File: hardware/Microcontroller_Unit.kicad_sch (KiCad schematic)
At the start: 30 parts

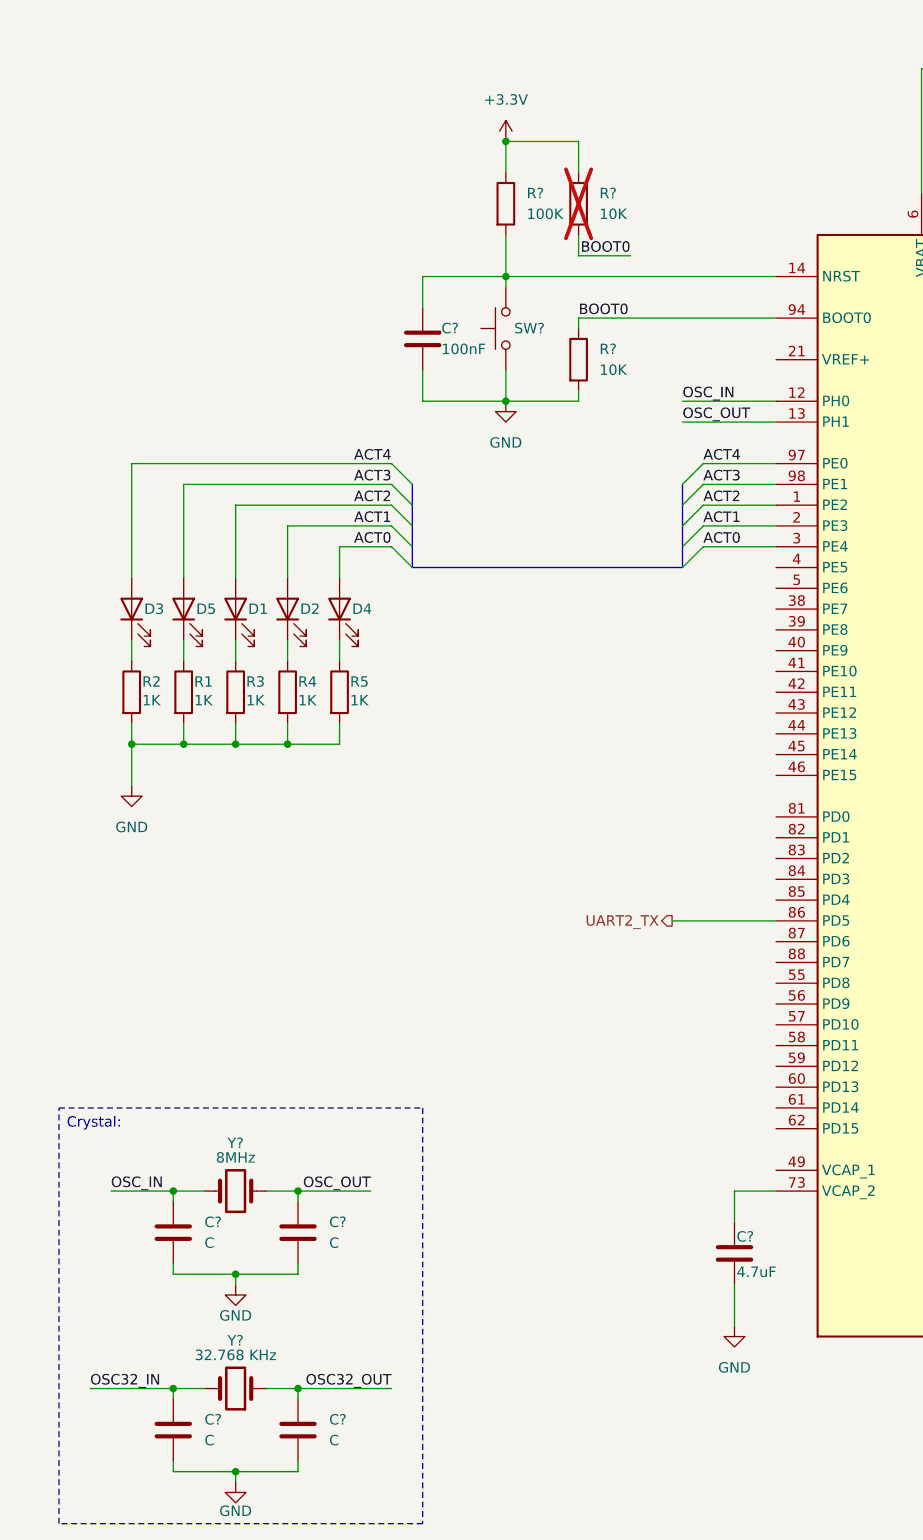
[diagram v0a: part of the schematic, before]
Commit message: Change ESP32 module to stand-alone, change regulator for wide input range, modify location of certain things on MCU_Unit.
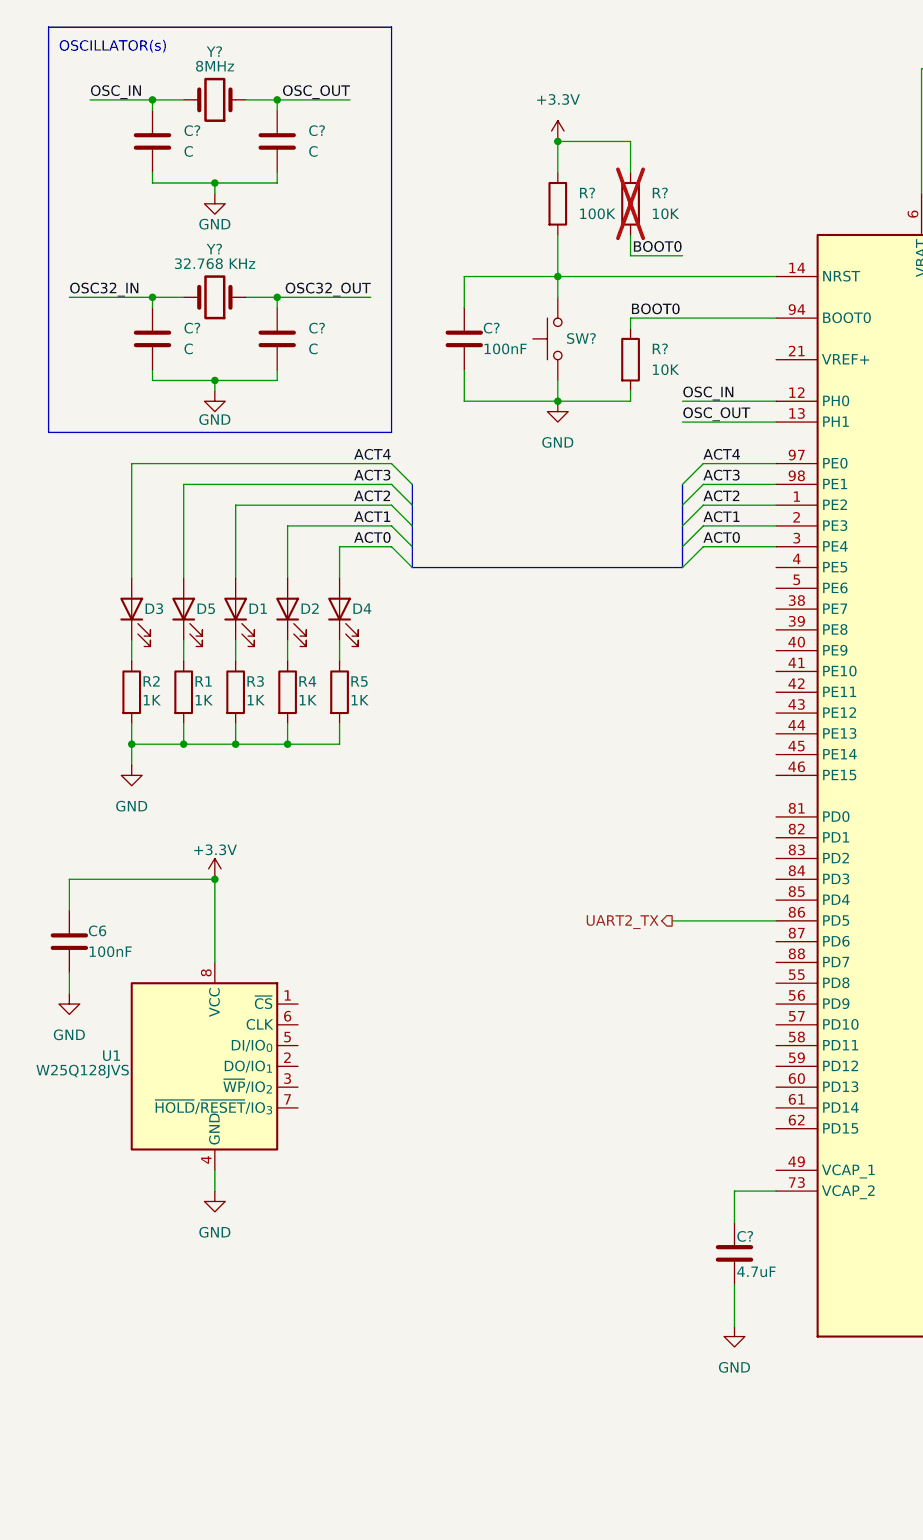
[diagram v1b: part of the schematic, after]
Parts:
- added C6: 100nF, Capacitor_SMD:C_0805_2012Metric_Pad1.18x1.45mm_HandSolder, symbol Device:C
- added R2: 1K, symbol Device:R
- added U1: W25Q128JVS, Package_SO:SOIC-8_5.3x5.3mm_P1.27mm, symbol Memory_Flash:W25Q128JVS
- R?: renamed from R2; value 1K -> 10K
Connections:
- net +3.3V: now also C6.1, U1.8 (VCC)
- net GND: now also C6.2, R2.2, U1.4 (GND)
- net at D3.1 (K): now also R2.1; no longer R?.1
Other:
- note added: "OSCILLATOR(s)"
- moved on the sheet: C?, R?, SW?, Y?

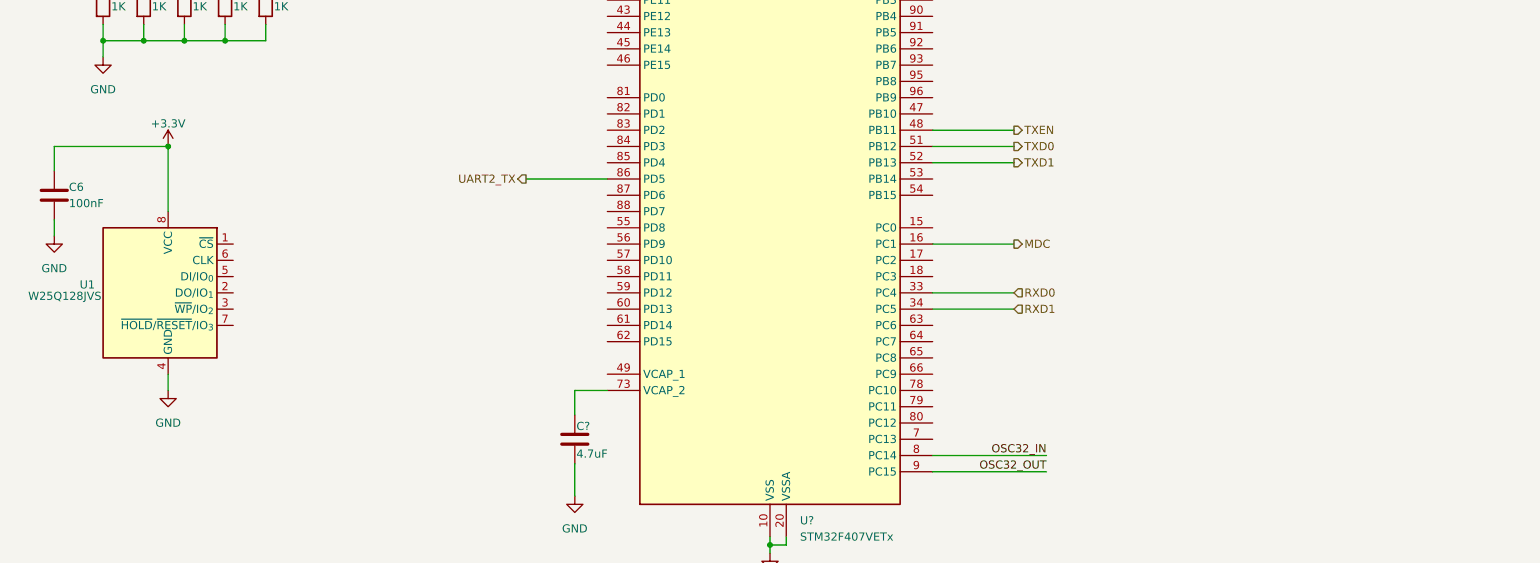
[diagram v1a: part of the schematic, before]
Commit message: Add Flash.
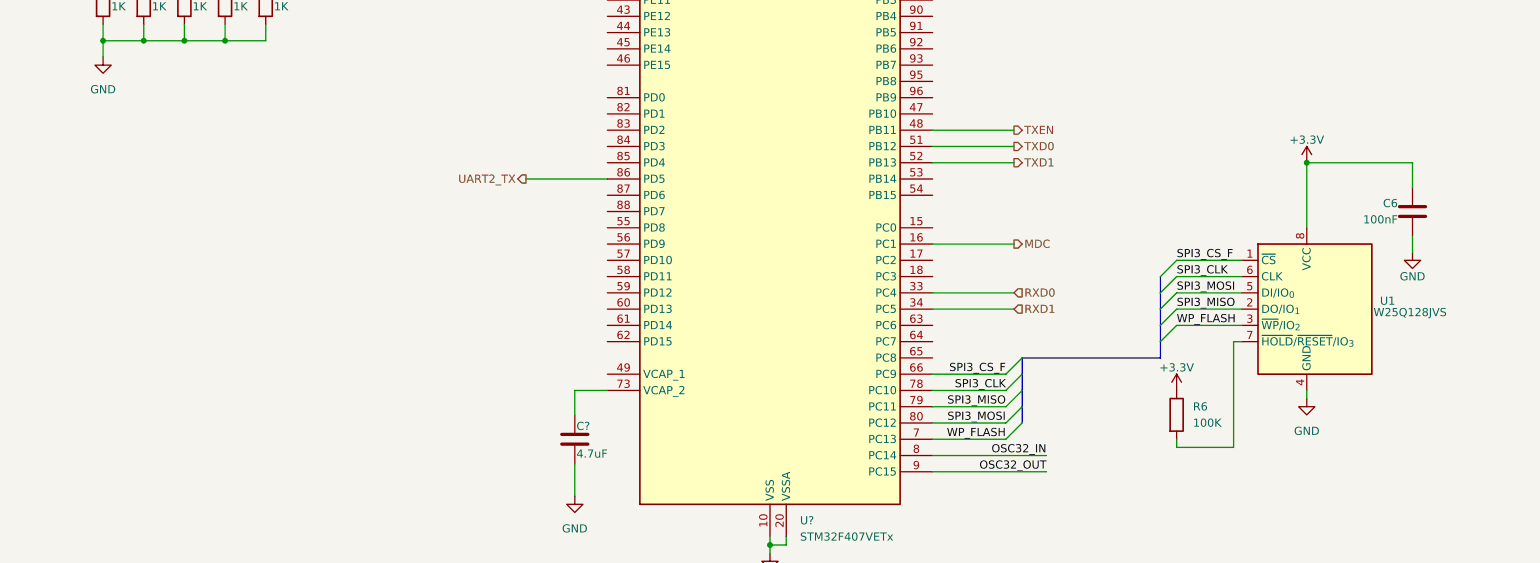
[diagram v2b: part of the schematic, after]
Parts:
- added R6: 100K, symbol Device:R
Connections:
- net +3.3V: now also R6.1
- net SPI3_CS_F: now reaches U?.66 (PC9)
- net SPI3_CS_F: now also U1.1 (~{CS})
- net WP_FLASH: now reaches U?.7 (PC13)
- net WP_FLASH: now also U1.3 (~{WP}/IO_{2})
- net SPI3_CLK: now reaches U?.78 (PC10)
- net SPI3_CLK: now also U1.6 (CLK)
- net SPI3_MISO: now reaches U?.79 (PC11)
- net SPI3_MISO: now also U1.2 (DO/IO_{1})
- net SPI3_MOSI: now reaches U?.80 (PC12)
- net SPI3_MOSI: now also U1.5 (DI/IO_{0})
- net at U1.7 (~{HOLD}/~{RESET}/IO_{3}): now also R6.2
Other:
- moved on the sheet: C6, U1

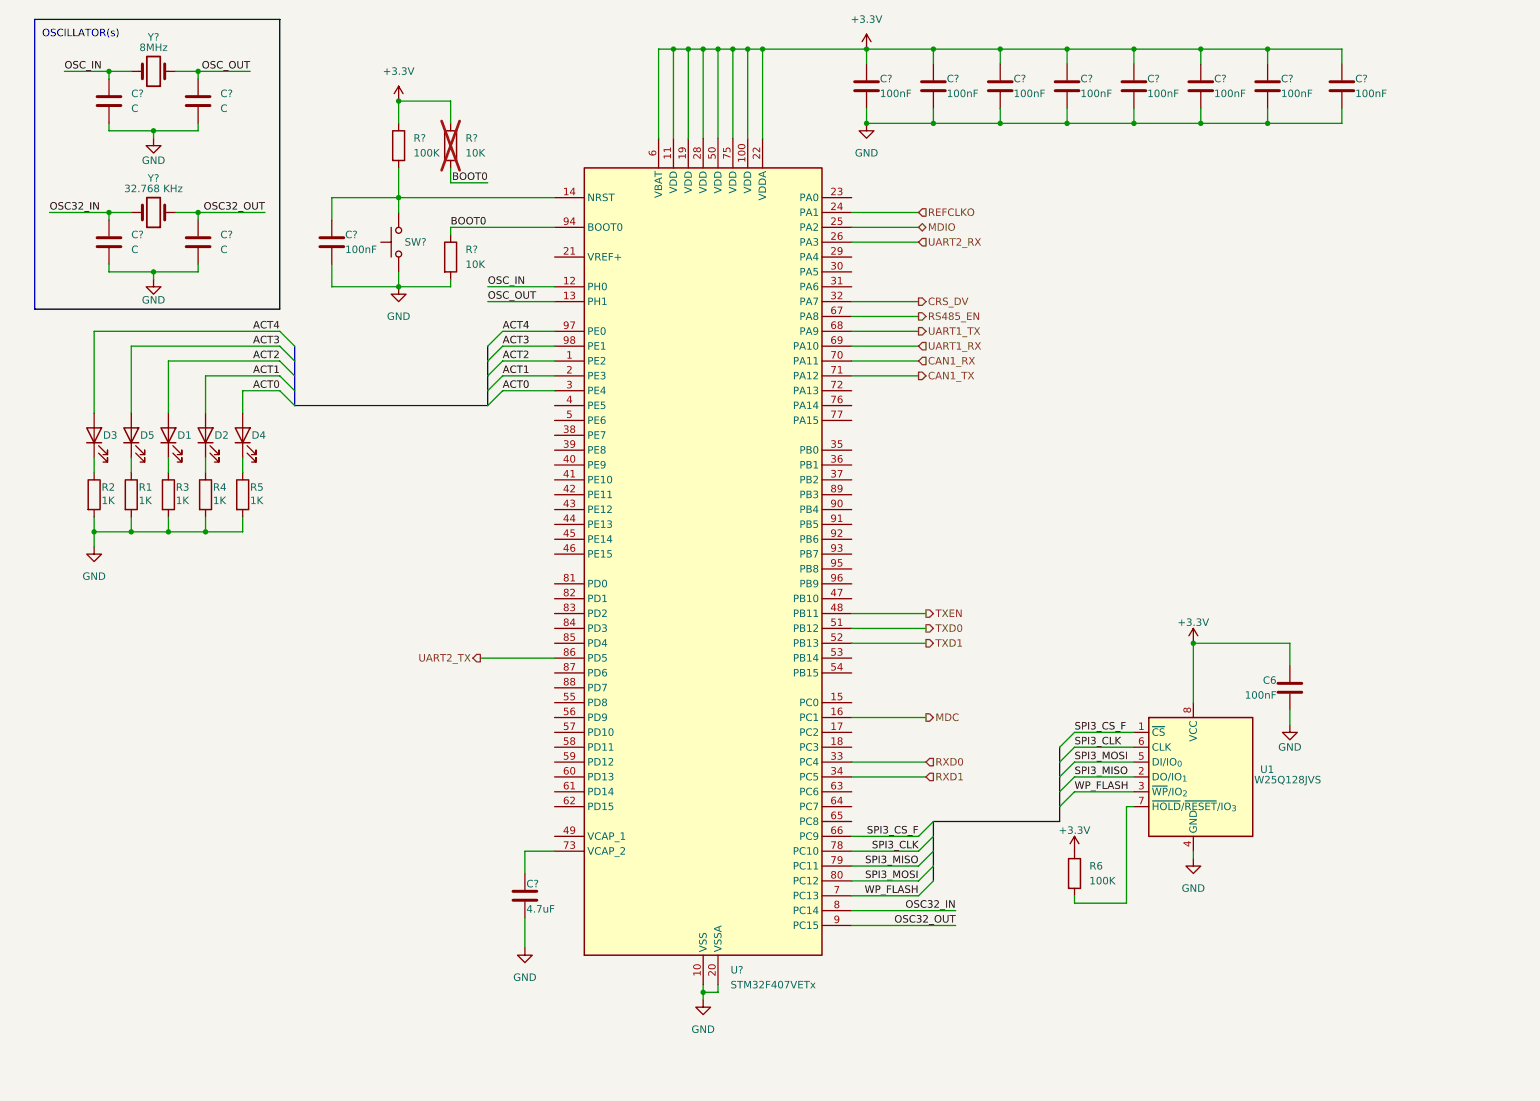
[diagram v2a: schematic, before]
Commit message: Assign footprints to some components and improvements.
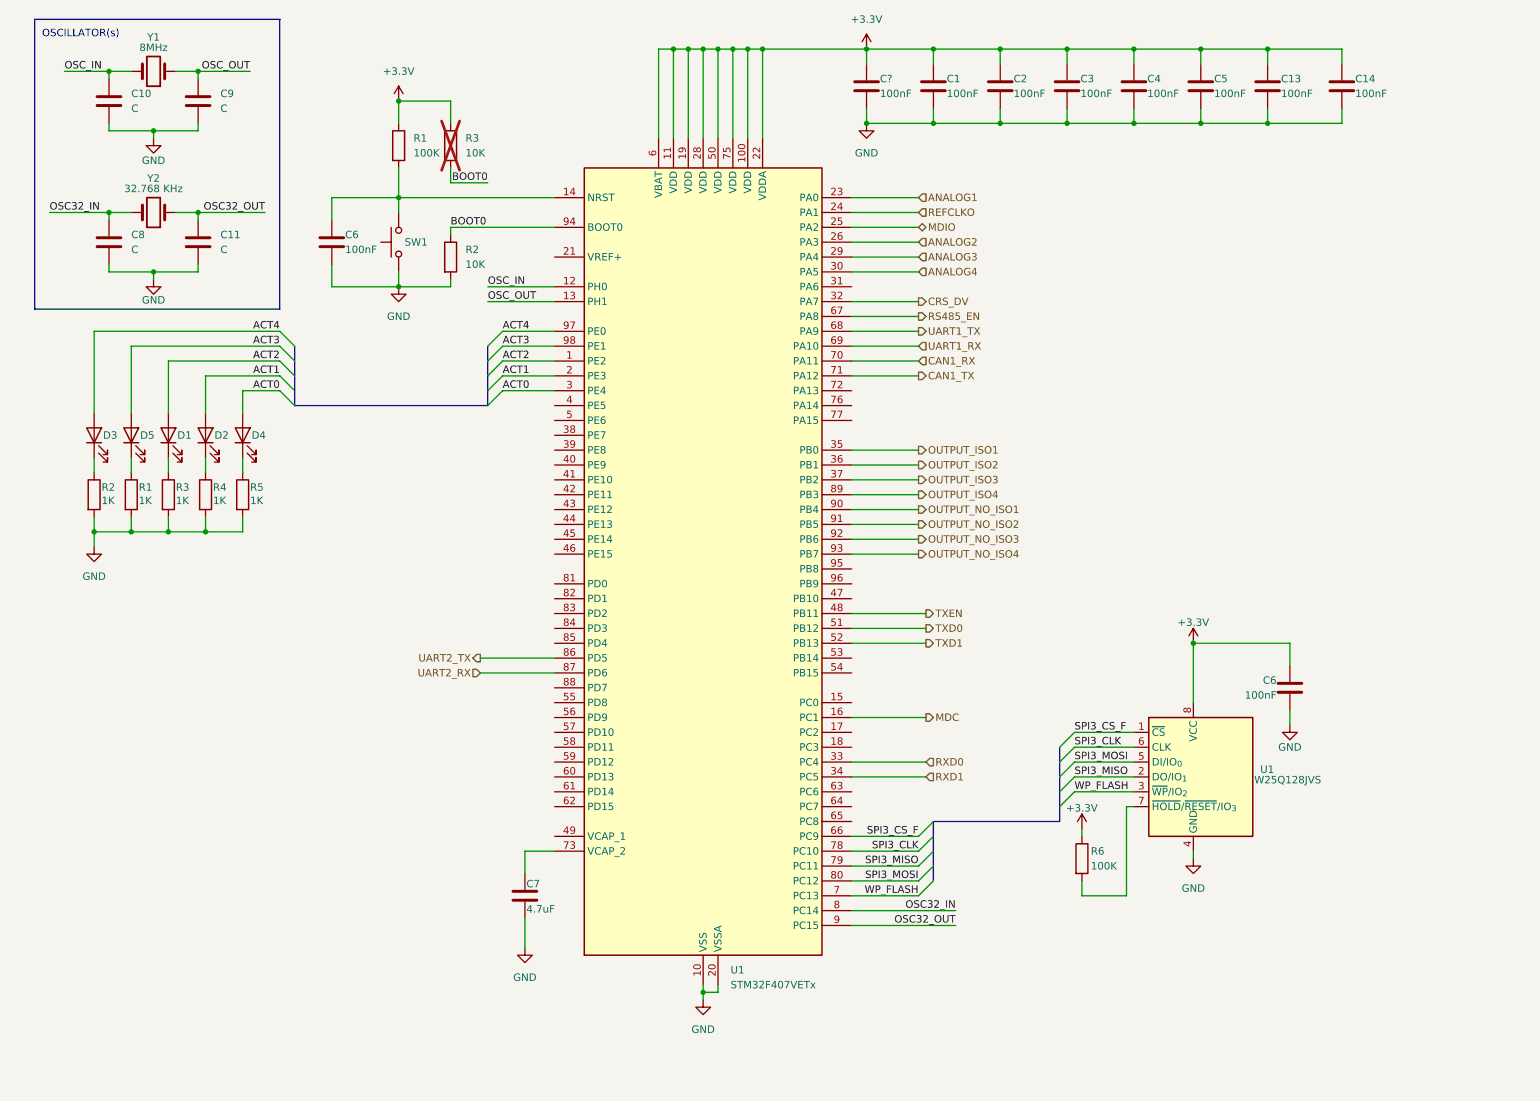
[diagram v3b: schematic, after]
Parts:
- R1, R2, R3, R4, R5, R6: footprint (none) -> Resistor_SMD:R_0805_2012Metric_Pad1.20x1.40mm_HandSolder
- R1, R2: renamed from R?; footprint (none) -> Resistor_SMD:R_0805_2012Metric_Pad1.20x1.40mm_HandSolder
- gave numbers to parts that had none: 18
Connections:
- net UART2_RX: now also U1.87 (PD6); no longer U1.26 (PA3)
- net ANALOG1: now reaches U1.23 (PA0)
- net ANALOG3: now reaches U1.29 (PA4)
- net ANALOG4: now reaches U1.30 (PA5)
- net OUTPUT_ISO1: now reaches U1.35 (PB0)
- net OUTPUT_ISO2: now reaches U1.36 (PB1)
- net OUTPUT_ISO3: now reaches U1.37 (PB2)
- net OUTPUT_ISO4: now reaches U1.89 (PB3)
- net OUTPUT_NO_ISO1: now reaches U1.90 (PB4)
- net OUTPUT_NO_ISO2: now reaches U1.91 (PB5)
- net OUTPUT_NO_ISO3: now reaches U1.92 (PB6)
- net OUTPUT_NO_ISO4: now reaches U1.93 (PB7)
- new net ANALOG2: U1.26 (PA3)
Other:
- moved on the sheet: R6

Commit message: Improvements to schematic.
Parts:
- added C? (x2): 100nF, Capacitor_SMD:C_0805_2012Metric_Pad1.18x1.45mm_HandSolder, symbol Device:C
- added C?: 2.2uF, Capacitor_SMD:C_0805_2012Metric_Pad1.18x1.45mm_HandSolder, symbol Device:C
- added C? (x2): 1uF, Capacitor_SMD:C_0805_2012Metric_Pad1.18x1.45mm_HandSolder, symbol Device:C
- added FB?: FerriteBead, symbol Device:FerriteBead
- C?: renamed from C7; value 4.7uF -> 2.2uF
- renumbered C13 to C?, C1 to C?, C2 to C?, C8 to C?, C9 to C?, C4 to C?, C11 to C?, C5 to C?, C10 to C?, C6 to C?, C14 to C?, C3 to C?, R2 to R?, R1 to R?, R3 to R?, SW1 to SW?, U1 to U?, Y1 to Y?, Y2 to Y?
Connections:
- net +3.3V: now also U?.21 (VREF+), C?.1, C?.1, FB?.2; no longer U?.22 (VDDA)
- net GND: now also C?.2, C?.2, C?.2, C?.2, C?.2
- net OUTPUT_NO_ISO1: now also U?.81 (PD0)
- net OUTPUT_NO_ISO2: now also U?.82 (PD1)
- net OUTPUT_NO_ISO3: now also U?.83 (PD2)
- net OUTPUT_NO_ISO4: now also U?.84 (PD3)
- net Digital_In_3: now reaches U?.38 (PE7)
- net Digital_In_4: now reaches U?.39 (PE8)
- net Digital_In_1: now reaches U?.4 (PE5)
- net DIG_IN_ISO_1: now reaches U?.43 (PE12)
- net DIG_IN_ISO_2: now reaches U?.44 (PE13)
- net DIG_IN_ISO_3: now reaches U?.45 (PE14)
- net DIG_IN_ISO_4: now reaches U?.46 (PE15)
- net at U?.49 (VCAP_1): now also C?.1
- net Digital_In_2: now reaches U?.5 (PE6)
- new net: C?.1, C?.1, FB?.1, U?.22 (VDDA)
- no-connect marks 0 -> 28
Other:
- moved on the sheet: C?, D1, D2, D3, D4, D5, R1, R2, R3, R4, R5, R?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
